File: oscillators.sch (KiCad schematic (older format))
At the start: 136 parts, among them U1 TL072-, U2 TL072-, U3 TL072-, U4 TA75S558F, U5 CD4052, U6 TL072-, U7 TL072-, U8 TL072-, U9 CD4052

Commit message: annotated, added decoupling caps
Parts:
- removed U2, U3, U7, U8: TL072-, MyModules:TSSOP8-JRL, symbol TL072-
- added U24, U27: TL074-, symbol TL074-
- gave numbers to parts that had none: 125
- renumbered U6 to U23, U4 to U25, U1 to U26, U5 to U30, U9 to U31
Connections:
- net VCO1_PUSLE is gone; now on net VCO1_PULSE: D10.1 (K), R230.2
- net VCO1_SQARE is gone; now on net VCO1_SQUARE: U30.4 (Y3)
- net +12V: now also U24.4 (V+), U27.4 (V+)
- net -12V: now also U24.11 (V-), U27.11 (V-)
- net GND: now also U24.3 (+), U27.3 (+)
- net SYNC: now also U24.6 (-)
- net at C29.2, D9.1 (K), Q29.1 (D)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: now also U27.1
- net at Q31.4 (C), R176.1: now also U27.2 (-)
- net at C27.1, D5.1 (K): now also U27.7
- net at C27.2, R187.2: now also U27.5 (+)
- net at C30.1, R169.2, R170.1: now also U27.6 (-)
- net at R226.1: now also U27.8
- net at R224.2: now also U27.9 (-)
- net at R228.2: now also U27.10 (+)
- net at R242.2, R243.1: now also U27.12 (+)
- net at R235.2: now also U27.13 (-)
- net at R232.1, R237.1, R244.2: now also U27.14
- net at C31.2, D12.1 (K), Q30.1 (D)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: now also U24.1
- net at Q32.4 (C), R178.1: now also U24.2 (-)
- net at C28.1, D6.1 (K): now also U24.7
- net at C28.2, R188.2: now also U24.5 (+)
- net at C34.1, R174.1, R184.1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: now also U24.9 (-)
- net at C34.2, R184.2, R197.1: now also U24.8
- net at D7.1 (K), D8.2 (A), R195.2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: now also U24.10 (+)
- net at R229.2: now also U24.12 (+)
- net at R225.2: now also U24.13 (-)
- net at R227.1, R236.1: now also U24.14

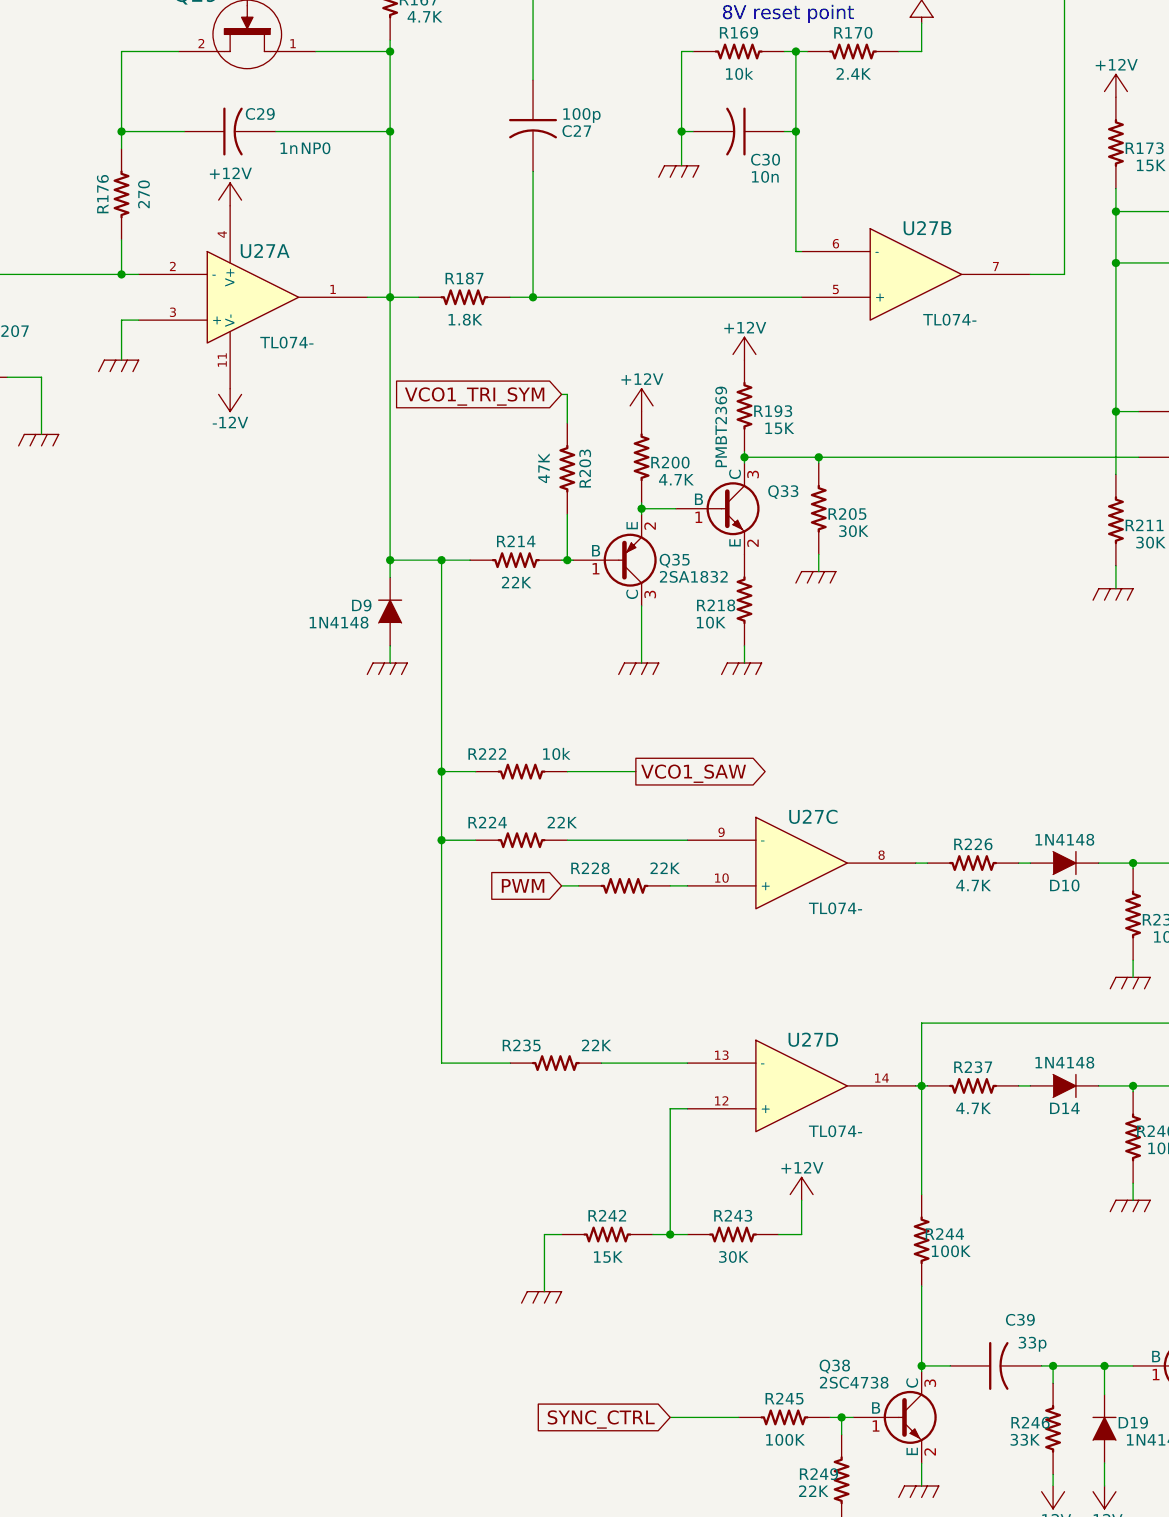
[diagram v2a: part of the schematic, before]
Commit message: starting placing VCO1
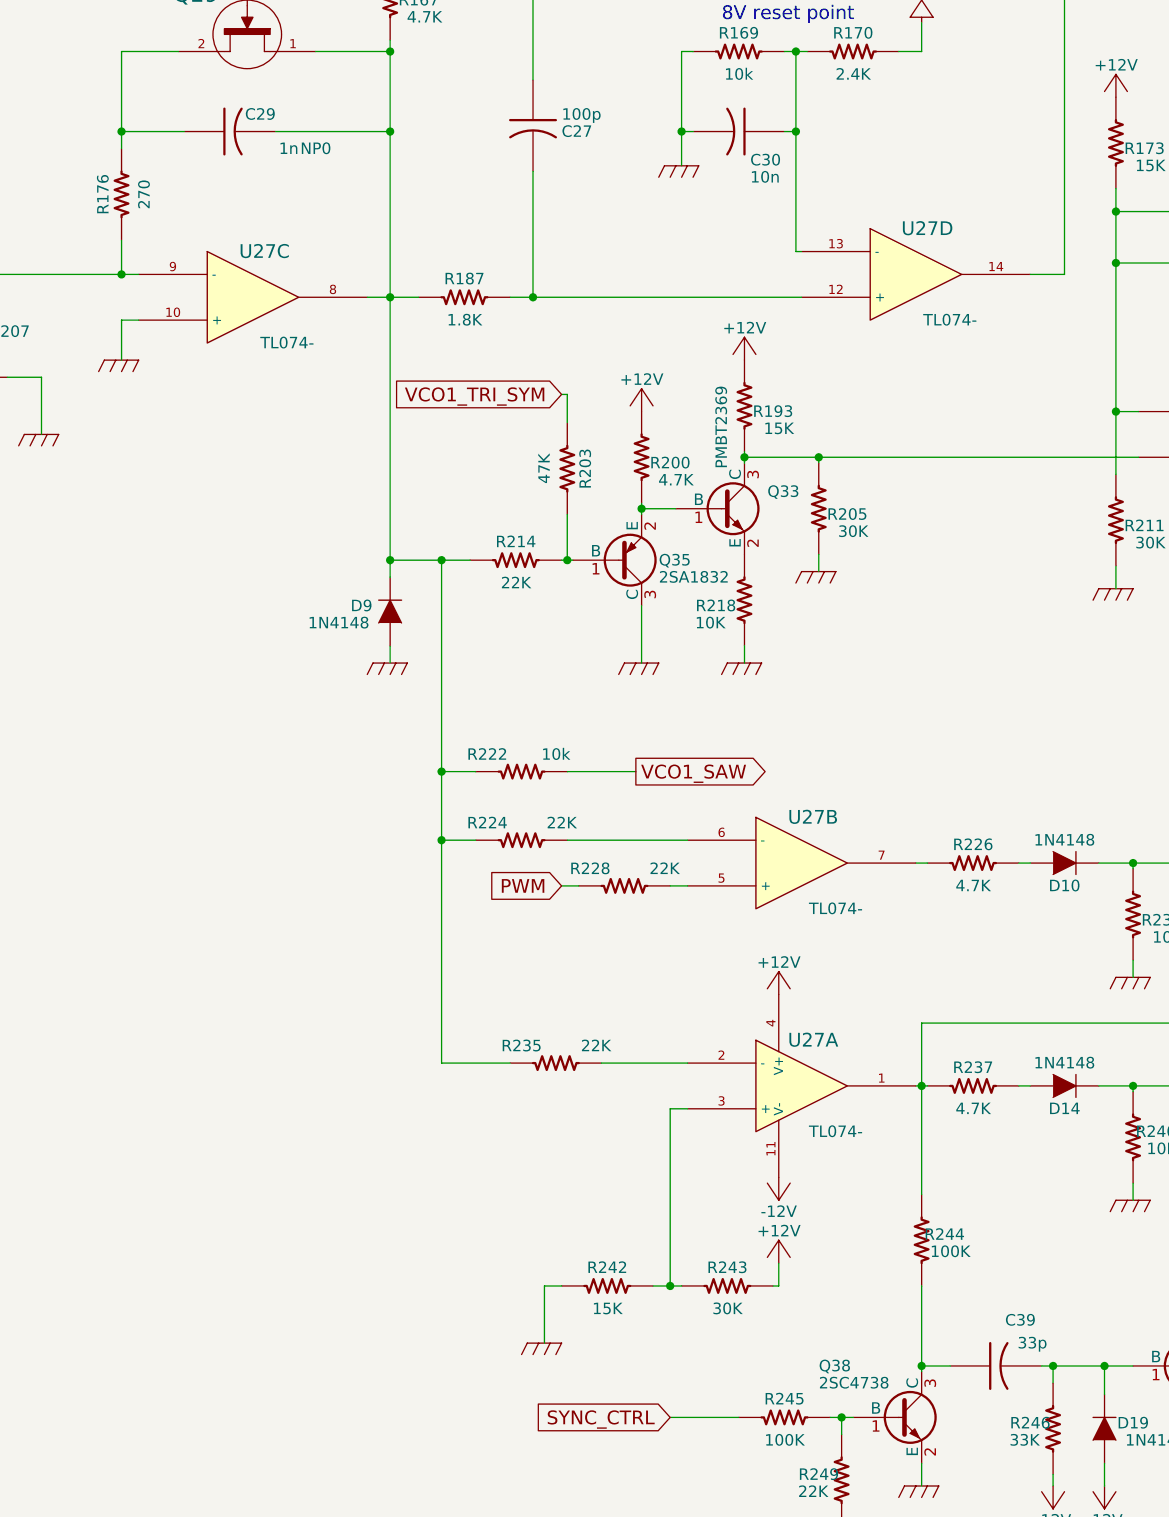
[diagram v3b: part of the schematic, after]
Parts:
- C27, C28, C30, C32, C33, C34, C39: footprint (none) -> MyModules:SM0603-C-JRL
- C29, C31: footprint (none) -> MyModules:SM0805-HAND-C
- D10, D11, D12, D13, D14, D15, D19, D5, D6, D7, D8, D9: footprint (none) -> MyModules:SOD323-C1A2
- Q29, Q30: footprint (none) -> MyModules:SOT23-132-JRL
- Q33, Q34, Q37: footprint SOT-23 -> MyModules:SOT23-132-JRL
- Q35, Q38: footprint SOT-23 -> MyModules:SOT416-SC75
- TC1, TC2: footprint (none) -> MyModules:SM0805-HAND
- U24, U27: footprint (none) -> Housings_SSOP:TSSOP-14_4.4x5mm_Pitch0.65mm
- U25: footprint (none) -> MyModules:SOT753_TSOP5_SC-74A
- U30, U31: footprint (none) -> MyModules:TSSOP-16_4.4x5mm_Pitch0.65mm_jrl
- VR1, VR2: footprint (none) -> MyModules:Bourns_3362P
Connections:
- net GND: now also U27.10 (+); no longer U27.3 (+)
- net at C29.2, D9.1 (K), Q29.1 (D)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: now also U27.8; no longer U27.1
- net at Q31.4 (C), R176.1: now also U27.9 (-); no longer U27.2 (-)
- net at C27.1, D5.1 (K): now also U27.14; no longer U27.7
- net at C27.2, R187.2: now also U27.12 (+); no longer U27.5 (+)
- net at C30.1, R169.2, R170.1: now also U27.13 (-); no longer U27.6 (-)
- net at R226.1: now also U27.7; no longer U27.8
- net at R224.2: now also U27.6 (-); no longer U27.9 (-)
- net at R228.2: now also U27.5 (+); no longer U27.10 (+)
- net at R235.2: now also U27.2 (-); no longer U27.13 (-)
- net at R242.2, R243.1: now also U27.3 (+); no longer U27.12 (+)
- net at R232.1, R237.1, R244.2: now also U27.1; no longer U27.14
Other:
- moved on the sheet: R242, R243, U27A, U27B, U27C, U27D

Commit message: first of many many days of routing
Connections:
- net at R226.1: now also U27.1; no longer U27.7
- net at R224.2: now also U27.2 (-); no longer U27.6 (-)
- net at R228.2: now also U27.3 (+); no longer U27.5 (+)
- net at R235.2: now also U27.6 (-); no longer U27.2 (-)
- net at R242.2, R243.1: now also U27.5 (+); no longer U27.3 (+)
- net at R232.1, R237.1, R244.2: now also U27.7; no longer U27.1
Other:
- moved on the sheet: U27A, U27B
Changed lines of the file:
@@
 L +12V #PWR0189
 U 1 1 5819C500
-P 10700 10950
-F 0 "#PWR0189" H 10700 10800 50  0001 C CNN
-F 1 "+12V" H 10700 11090 50  0000 C CNN
-F 2 "" H 10700 10950 60  0000 C CNN
-F 3 "" H 10700 10950 60  0000 C CNN
-	1    10700 10950
+P 10700 9975
+F 0 "#PWR0189" H 10700 9825 50  0001 C CNN
+F 1 "+12V" H 10700 10115 50  0000 C CNN
+F 2 "" H 10700 9975 60  0000 C CNN
+F 3 "" H 10700 9975 60  0000 C CNN
+	1    10700 9975
 	1    0    0    -1
 $EndComp
@@
 L -12V #PWR0190
 U 1 1 5819C506
-P 10700 11750
-F 0 "#PWR0190" H 10700 11850 30  0001 C CNN
-F 1 "-12V" H 10700 11900 50  0000 C CNN
-F 2 "~" H 10700 11750 60  0000 C CNN
-F 3 "~" H 10700 11750 60  0000 C CNN
-	1    10700 11750
+P 10700 10775
+F 0 "#PWR0190" H 10700 10875 30  0001 C CNN
+F 1 "-12V" H 10700 10925 50  0000 C CNN
+F 2 "~" H 10700 10775 60  0000 C CNN
+F 3 "~" H 10700 10775 60  0000 C CNN
+	1    10700 10775
 	-1   0    0    1
 $EndComp
@@
 L TL074- U27
 U 2 1 5A72E489
-P 10800 10375
-F 0 "U27" H 10850 10575 60  0000 C CNN
-F 1 "TL074-" H 10950 10175 50  0000 C CNN
-F 2 "Housings_SSOP:TSSOP-14_4.4x5mm_Pitch0.65mm" H 10800 10375 60  0001 C CNN
-F 3 "" H 10800 10375 60  0000 C CNN
-	2    10800 10375
-	1    0    0    -1
-$EndComp
-$Comp
-L TL074- U27
-U 1 1 5A72EF39
 P 10800 11350
 F 0 "U27" H 10850 11550 60  0000 C CNN
@@
 F 2 "Housings_SSOP:TSSOP-14_4.4x5mm_Pitch0.65mm" H 10800 11350 60  0001 C CNN
 F 3 "" H 10800 11350 60  0000 C CNN
-	1    10800 11350
+	2    10800 11350
+	1    0    0    -1
+$EndComp
+$Comp
+L TL074- U27
+U 1 1 5A72EF39
+P 10800 10375
+F 0 "U27" H 10850 10575 60  0000 C CNN
+F 1 "TL074-" H 10950 10175 50  0000 C CNN
+F 2 "Housings_SSOP:TSSOP-14_4.4x5mm_Pitch0.65mm" H 10800 10375 60  0001 C CNN
+F 3 "" H 10800 10375 60  0000 C CNN
+	1    10800 10375
 	1    0    0    -1
 $EndComp

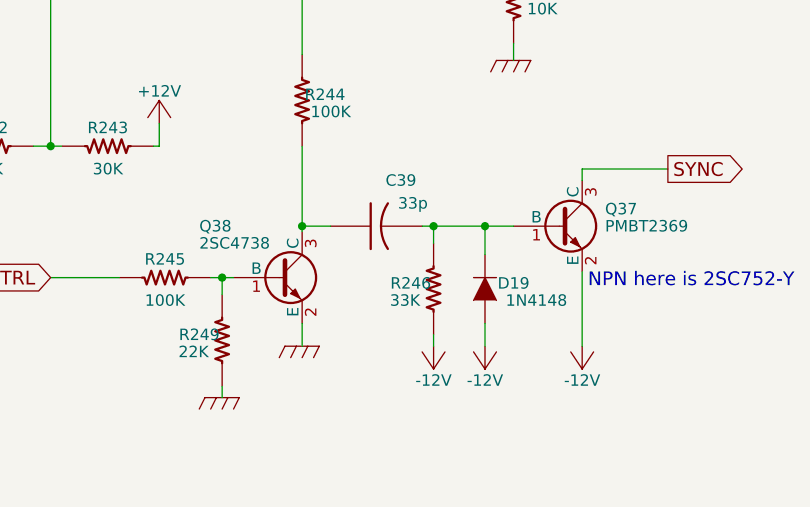
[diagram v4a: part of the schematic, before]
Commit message: VCO1 mostly placed
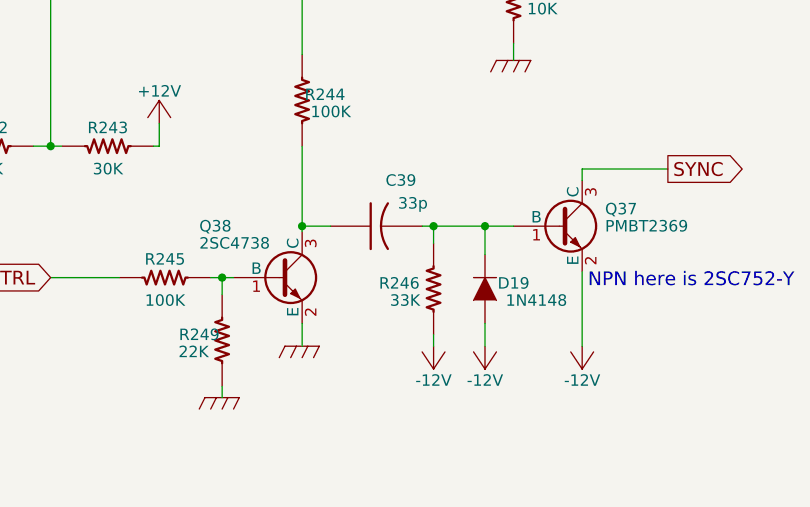
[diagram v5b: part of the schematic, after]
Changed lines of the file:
@@
 U 1 1 5819C6AE
 P 11900 12850
-F 0 "R246" H 11800 12825 50  0000 C CNN
+F 0 "R246" H 11750 12825 50  0000 C CNN
 F 1 "33K" H 11775 12900 50  0000 C CNN
 F 2 "MyModules:SM0603-R-JRL" H 11900 12850 60  0001 C CNN

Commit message: placing
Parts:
- removed VR1, VR2: 20K, MyModules:Bourns_3362P, symbol POT_US
- added R250, R251: 10K, MyModules:SM0603-R-JRL, symbol R_US
- added TP10, TP11, TP12, TP13: TEST_POINT, MyModules:TEST_POINT_SMALL, symbol TEST_POINT
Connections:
- net -5V: now also U30.7 (VEE), U31.7 (VEE); no longer U30.8 (VSS), U31.8 (VSS)
- net GND: now also U30.8 (VSS), U31.8 (VSS); no longer U30.7 (VEE), U31.7 (VEE)
- net VCO1_SAW: now also U30.4 (Y3); no longer U30.5 (Y1)
- net VCO1_SQUARE: now also U30.1 (Y0); no longer U30.4 (Y3)
- net VCO1_TRI: now also U30.5 (Y1); no longer U30.1 (Y0)
- net VCO1_XMOD: now also R250.2, TP12.1
- net at R181.1: now also R250.1, TP10.1
- net at C36.2, R190.1, R199.2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: now also R251.2, TP13.1
- net at R183.1: now also R251.1, TP11.1
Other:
- note removed: "ideally replace pot \nwith fixed resistor"
